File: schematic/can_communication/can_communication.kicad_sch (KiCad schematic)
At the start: 0 parts

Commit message: Added STM32H723ZGT
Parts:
- added U1: STM32H723ZGTx, Package_QFP:LQFP-144_20x20mm_P0.5mm, symbol MCU_ST_STM32H7:STM32H723ZGTx
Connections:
- new net: U1.107 (VSS), U1.120 (VSS), U1.130 (VSS), U1.16 (VSS), U1.38 (VSS), U1.51 (VSS), U1.61 (VSS), U1.83 (VSS), U1.94 (VSS)
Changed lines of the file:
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@@
 	(generator_version "9.0")
 	(paper "A4")
-	(sheet_instances
-		(path "/"
-			(page "1")
-		)
-	)
-	(embedded_fonts no)
-)

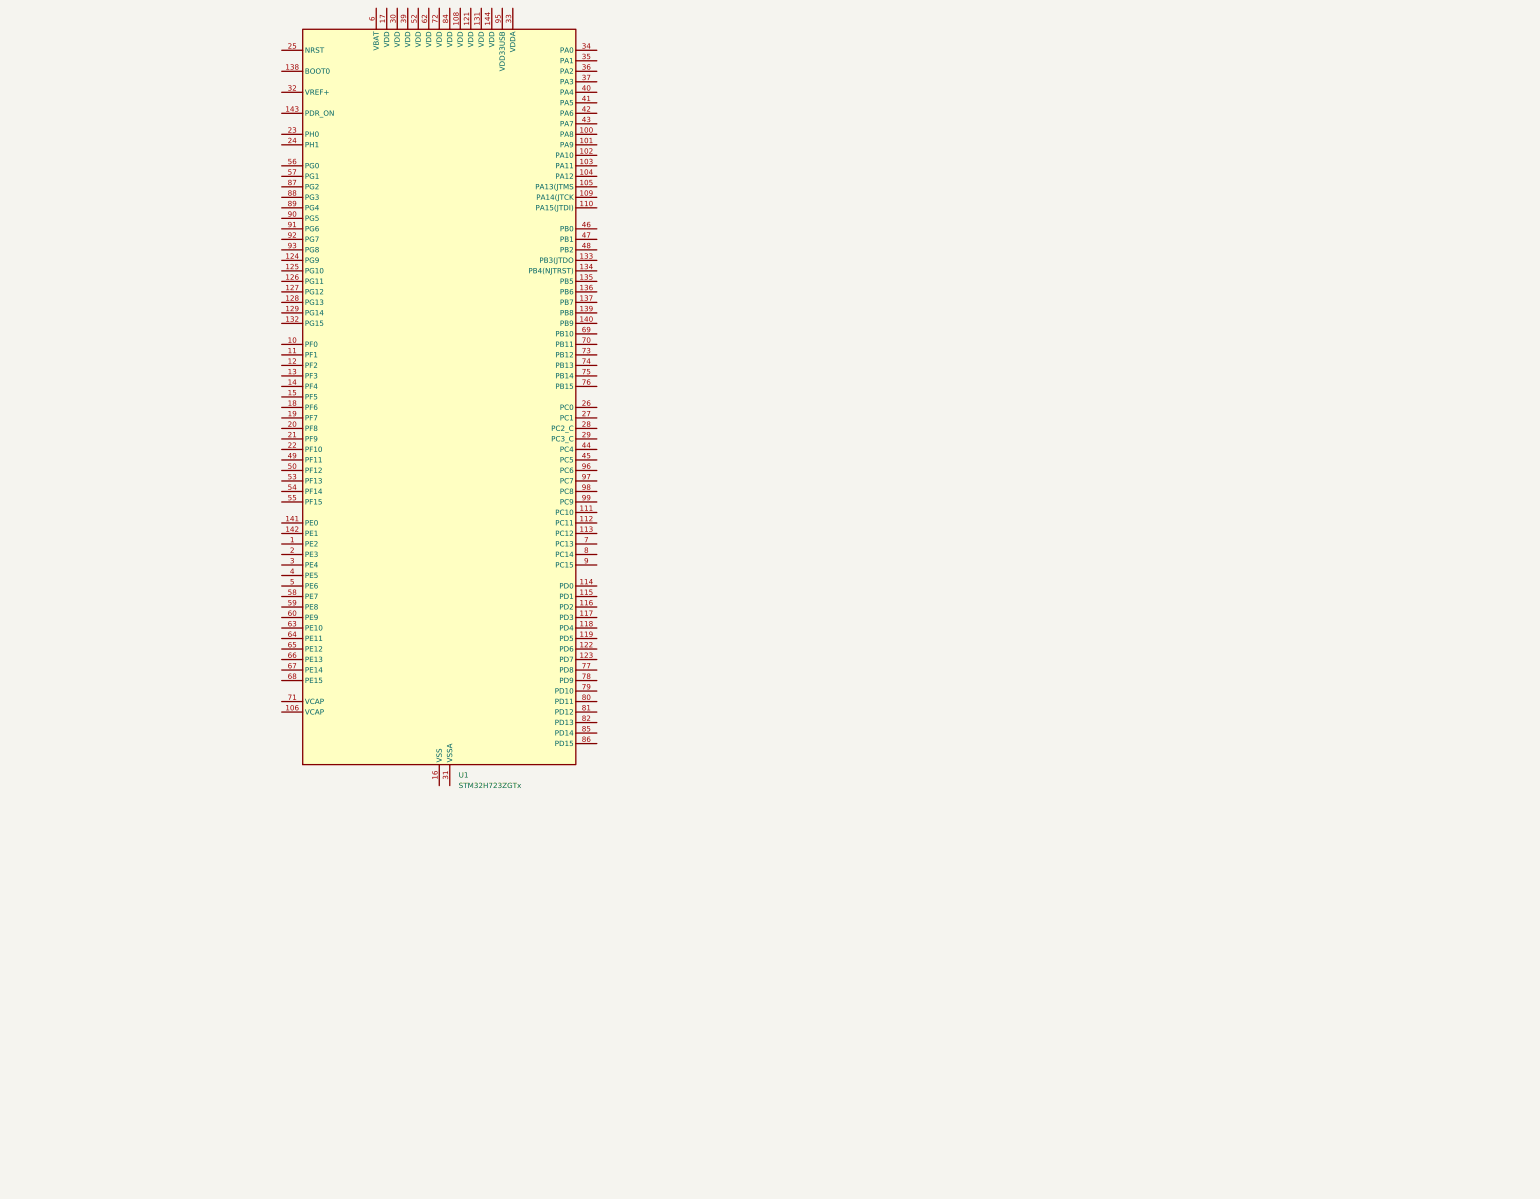
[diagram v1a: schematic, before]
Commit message: added stm32 program
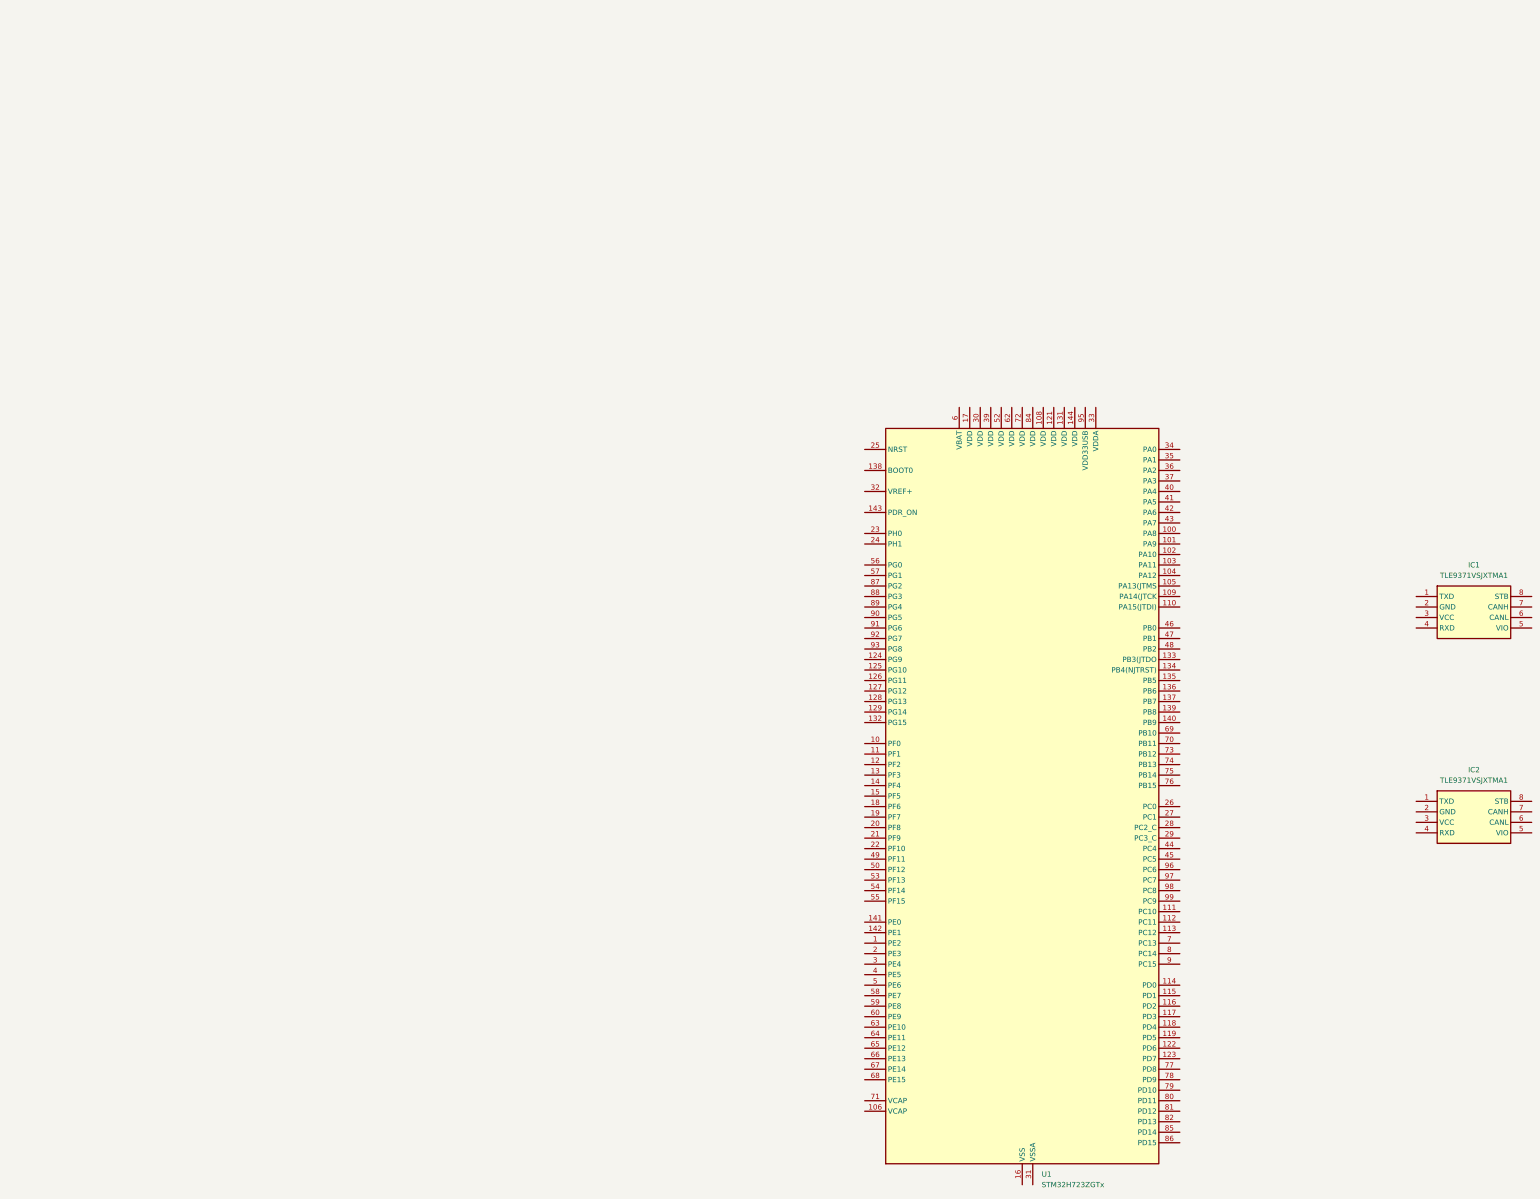
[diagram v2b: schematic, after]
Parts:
- added IC1, IC2: TLE9371VSJXTMA1, TLE9371VSJXTMA1:SOIC127P602X173-8N, symbol TLE9371VSJXTMA1:TLE9371VSJXTMA1
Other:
- company: (none) -> Jachan
- title: (none) -> Microcontroller
- moved on the sheet: U1
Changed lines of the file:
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@@
 	(generator "eeschema")
 	(generator_version "9.0")
-	(paper "A4")
+	(paper "A2")
+	(title_block
+		(title "Microcontroller")
+		(date "2025-10-29")
+		(rev "1")
+		(company "Jachan")
+	)

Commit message: add can communication devices
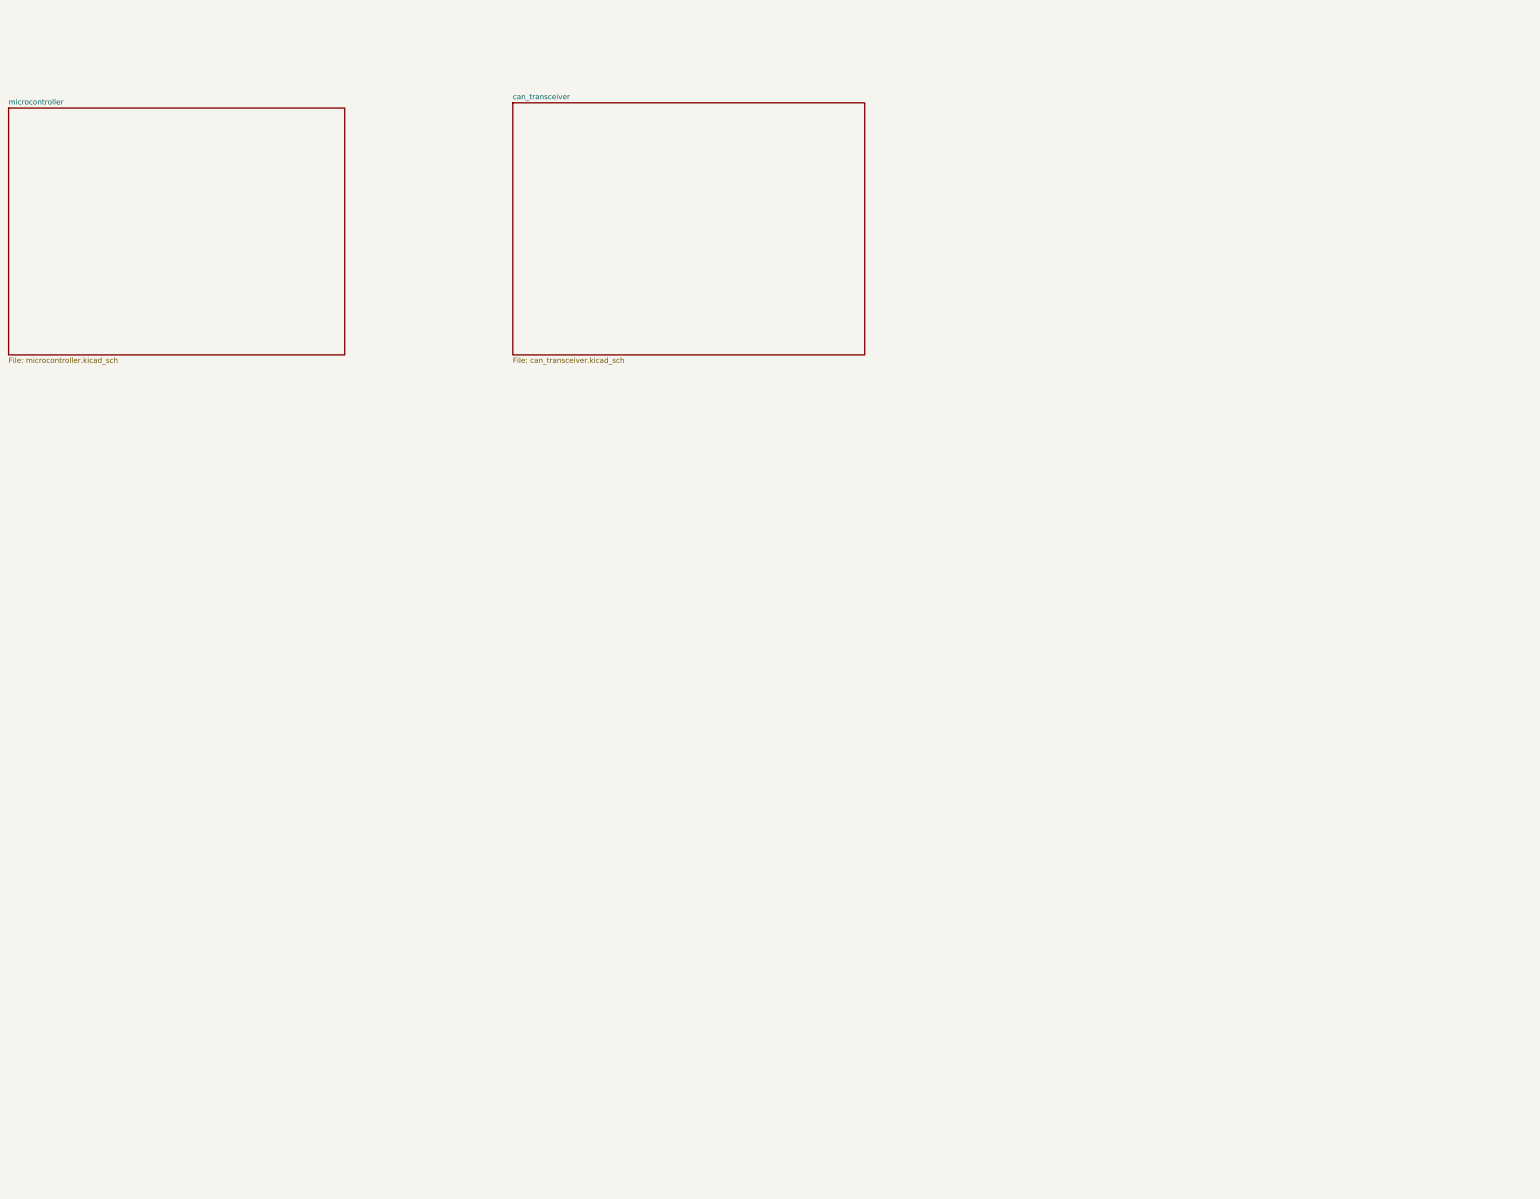
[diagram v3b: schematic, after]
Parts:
- removed IC1, IC2: TLE9371VSJXTMA1, TLE9371VSJXTMA1:SOIC127P602X173-8N, symbol TLE9371VSJXTMA1:TLE9371VSJXTMA1
- removed U1: STM32H723ZGTx, Package_QFP:LQFP-144_20x20mm_P0.5mm, symbol MCU_ST_STM32H7:STM32H723ZGTx
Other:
- added sheet can_transceiver (can_transceiver.kicad_sch)
- added sheet microcontroller (microcontroller.kicad_sch)
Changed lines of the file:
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@@
 		(company "Jachan")
 	)
+	(sheet
+		(at 146.05 33.02)
+		(size 85.09 60.96)
+		(exclude_from_sim no)
+		(in_bom yes)
+		(on_board yes)
+		(dnp no)
+		(fields_autoplaced yes)
+		(stroke
+			(width 0.1524)
+			(type solid)
+		)
+		(fill
+			(color 0 0 0 0.0000)
+		)
+		(property "Sheetname" "can_transceiver"
+			(at 146.05 32.3084 0)
+			(effects
+				(font
+					(size 1.27 1.27)
+				)
+				(justify left bottom)
+			)
+		)
+		(property "Sheetfile" "can_transceiver.kicad_sch"
+			(at 146.05 94.5646 0)
+			(effects
+				(font
+					(size 1.27 1.27)
+				)
+				(justify left top)
+			)
+		)
+		(instances
+			(project "can_communication"
+				(path "/7f1c7c45-fa4b-4772-81d9-7338c977dadb"
+					(page "3")
+				)
+			)
+		)
+	)
+	(sheet
+		(at 24.13 34.29)
+		(size 81.28 59.69)
+		(exclude_from_sim no)
+		(in_bom yes)
+		(on_board yes)
+		(dnp no)
+		(fields_autoplaced yes)
+		(stroke
+			(width 0.1524)
+			(type solid)
+		)
+		(fill
+			(color 0 0 0 0.0000)
+		)
+		(property "Sheetname" "microcontroller"
+			(at 24.13 33.5784 0)
+			(effects
+				(font
+					(size 1.27 1.27)
+				)
+				(justify left bottom)
+			)
+		)
+		(property "Sheetfile" "microcontroller.kicad_sch"
+			(at 24.13 94.5646 0)
+			(effects
+				(font
+					(size 1.27 1.27)
+				)
+				(justify left top)
+			)
+		)
+		(instances
+			(project "can_communication"
+				(path "/7f1c7c45-fa4b-4772-81d9-7338c977dadb"
+					(page "2")
+				)
+			)
+		)
+	)
+	(sheet_instances
+		(path "/"
+			(page "1")
+		)
+	)
+	(embedded_fonts no)
+)

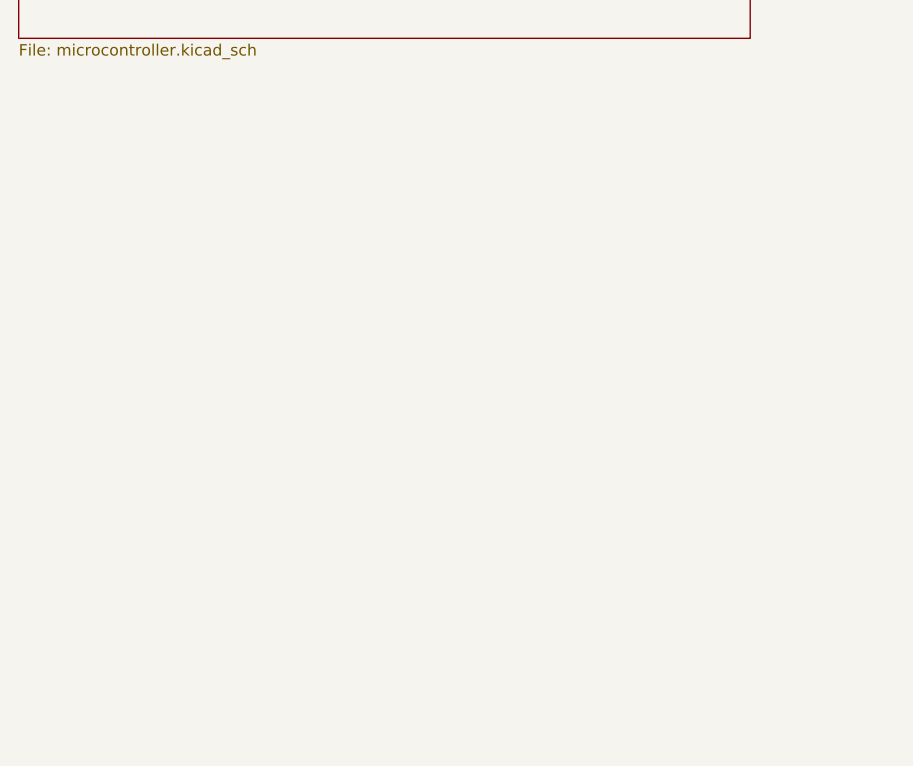
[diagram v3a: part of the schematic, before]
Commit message: added usb connectors
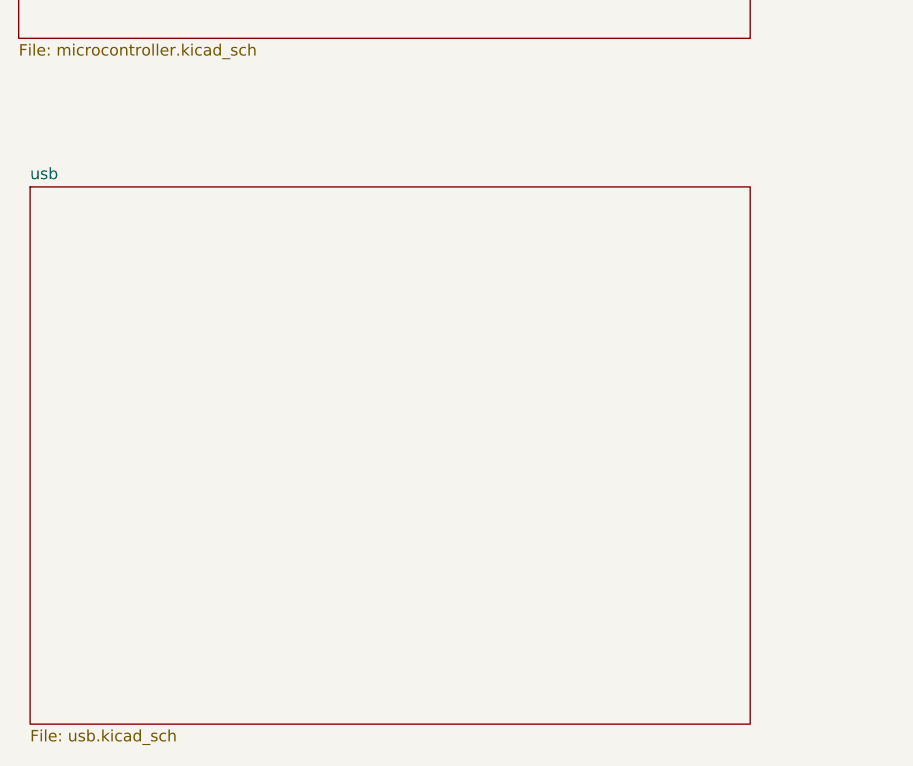
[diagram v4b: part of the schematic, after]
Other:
- added sheet usb (usb.kicad_sch)
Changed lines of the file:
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@@
+	)
+	(sheet
+		(at 25.4 110.49)
+		(size 80.01 59.69)
+		(exclude_from_sim no)
+		(in_bom yes)
+		(on_board yes)
+		(dnp no)
+		(fields_autoplaced yes)
+		(stroke
+			(width 0.1524)
+			(type solid)
+		)
+		(fill
+			(color 0 0 0 0.0000)
+		)
+		(property "Sheetname" "usb"
+			(at 25.4 109.7784 0)
+			(effects
+				(font
+					(size 1.27 1.27)
+				)
+				(justify left bottom)
+			)
+		)
+		(property "Sheetfile" "usb.kicad_sch"
+			(at 25.4 170.7646 0)
+			(effects
+				(font
+					(size 1.27 1.27)
+				)
+				(justify left top)
+			)
+		)
+		(instances
+			(project "can_communication"
+				(path "/7f1c7c45-fa4b-4772-81d9-7338c977dadb"
+					(page "4")
+				)
+			)
+		)
 	)
 	(sheet
